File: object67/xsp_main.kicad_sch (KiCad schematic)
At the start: 66 parts, among them IC5 TPS7A4701RGWT, IC6 TPS7A3301RGWR, J2 PJ-037A, J3 Power In, J4 216700-0249, U10 ADP5070AREZ, U11 TPS62912, U7 TPS7A2050PDQNR, U8 TPS7A2033PDQNR, U9 TPS7A2033PDQNR

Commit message: Finished layout
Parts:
- added H1: MountingHole_Pad, MountingHole:MountingHole_4.3mm_M4_ISO7380_Pad_TopOnly, symbol Mechanical:MountingHole_Pad
- C59, C60, C62, C63, C64, C65, C67, C68, C69, C71, C75, C76, C77: footprint (none) -> Capacitor_SMD:C_0603_1608Metric
- C61, C66, C70: value 47u -> 10u; footprint (none) -> Capacitor_SMD:C_0603_1608Metric
- C72, C88, C89, C90, C92, C93: footprint (none) -> Capacitor_SMD:C_1206_3216Metric
- C73, C74, C80, C91: footprint (none) -> Capacitor_SMD:C_0402_1005Metric
- C78, C79, C81, C82, C83, C84, C85, C86, C87: footprint (none) -> Capacitor_SMD:C_0805_2012Metric
- D1, D2: footprint (none) -> Diode_SMD:D_PowerDI-123
- FB4: footprint (none) -> Inductor_SMD:L_0603_1608Metric
- J3: footprint (none) -> Connector_PinHeader_2.54mm:PinHeader_1x01_P2.54mm_Vertical
- J4: footprint 2167000249 -> object67:2167000249
- L1, L2, L3: footprint (none) -> Inductor_SMD:L_Wuerth_MAPI-4030
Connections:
- net +3.3V: now also J4.16, J4.17, J4.18, J4.19, J4.20
- net BICK_{ADC}: now also J4.7
- net BICK_{DAC}: now also J4.2
- net CLK_44.1_EN: now also J4.12
- net CLK_48_EN: now also J4.13
- net CLK_EN: now also J4.11
- net GNDD: now also J4.14, J4.15, J4.21, J4.22, J4.23, J4.24, J4.25 (MP_1), J4.26 (MP_2), J4.27 (MP_3), J4.28 (MP_4), J4.29 (MP_5), J4.30 (MP_6)
- net GNDPWR: now also H1.1
- net INT_{ADC}: now also J4.10
- net LRCK_{ADC}: now also J4.8
- net LRCK_{DAC}: now also J4.4
- net PDN_{DAC}: now also J4.1
- net SCL: now also J4.5
- net SDA: now also J4.6
- net SDATA_{ADC}: now also J4.9
- net SDATA_{DAC}: now also J4.3
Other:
- moved on the sheet: J4

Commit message: Start layout
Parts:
- added J5: 216700-0249, object67:2167000249, symbol object67:216700-0249
- added J6: Conn_02x08_Odd_Even, Connector_PinHeader_2.54mm:PinHeader_2x08_P2.54mm_Horizontal, symbol Connector_Generic:Conn_02x08_Odd_Even
- J3: footprint Connector_PinHeader_2.54mm:PinHeader_1x01_P2.54mm_Vertical -> TestPoint:TestPoint_2Pads_Pitch5.08mm_Drill1.3mm
- R35, R36, R37, R38, R39, R40, R42, R43, R44, R45: footprint (none) -> Resistor_SMD:R_0805_2012Metric
- R41: footprint (none) -> Resistor_SMD:R_0603_1608Metric
- TP1, TP2, TP3, TP4: footprint (none) -> TestPoint:TestPoint_Pad_D2.0mm
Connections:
- net +3.3V: now also J4.1, J4.2, J4.3, J4.4, J5.1, J5.16, J5.17, J5.2, J6.1 (Pin_1), J6.2 (Pin_2), J6.3 (Pin_3); no longer J4.19, J4.20
- net BICK_{ADC}: now also J5.3, J6.4 (Pin_4); no longer J4.7
- net BICK_{DAC}: now also J4.6, J6.7 (Pin_7); no longer J4.2
- net CLK_44.1_EN: now also J5.19, J6.14 (Pin_14); no longer J4.12
- net CLK_48_EN: now also J5.20, J6.16 (Pin_16); no longer J4.13
- net CLK_EN: now also J5.18, J6.12 (Pin_12); no longer J4.11
- net GNDD: now also J4.10, J4.11, J4.12, J4.13, J5.10, J5.11, J5.12, J5.13, J5.14, J5.15, J5.21, J5.22, J5.23, J5.24, J5.7, J5.8, J5.9, J6.15 (Pin_15); no longer J4.25 (MP_1), J4.26 (MP_2), J4.27 (MP_3), J4.28 (MP_4), J4.29 (MP_5), J4.30 (MP_6)
- net INT_{ADC}: now also J5.6, J6.10 (Pin_10); no longer J4.10
- net LRCK_{ADC}: now also J5.4, J6.6 (Pin_6); no longer J4.8
- net LRCK_{DAC}: now also J4.8, J6.11 (Pin_11); no longer J4.4
- net PDN_{DAC}: now also J4.5, J6.5 (Pin_5); no longer J4.1
- net SCL: now also J4.19; no longer J4.5
- net SDA: now also J4.20; no longer J4.6
- net SDATA_{ADC}: now also J5.5, J6.8 (Pin_8); no longer J4.9
- net SDATA_{DAC}: now also J4.7, J6.9 (Pin_9); no longer J4.3
- new net MLCK_{MCU}: J4.9, J6.13 (Pin_13)
- no-connect marks 22 -> 34

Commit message: Updated pcb
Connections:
- net GNDD is gone; now on net GND: C67.2, C68.2, C69.2, C70.2, C71.1, C73.1, C74.1, C75.2, J4.10, J4.11, J4.12, J4.13, J4.14, J4.15, J4.21, J4.22, J4.23, J4.24, J5.10, J5.11, J5.12, J5.13, J5.14, J5.15, J5.21, J5.22, J5.23, J5.24, J5.7, J5.8, J5.9, J6.15 (Pin_15), R38.1, U10.15 (AGND), U10.21 (AGND), U10.4 (SYNC/FREQ), U9.2 (GND), U9.5 (Pad)
- net GNDPWR is gone; now on net GND: C72.1, C76.1, C77.1, C78.1, C79.1, C80.1, C81.1, C82.1, C83.1, C84.1, C85.1, C86.1, H1.1, J2.1, J3.2 (Pin_2), L2.1, R41.1, R43.1, U10.1 (PGND), U11.4 (PGND), U11.7 (PSNS)
- net GNDA renamed GND

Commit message: Layout for ADP5070
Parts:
- C72: footprint Capacitor_SMD:C_1206_3216Metric -> Capacitor_SMD:C_0805_2012Metric
- C73, C74: footprint Capacitor_SMD:C_0402_1005Metric -> Capacitor_SMD:C_0603_1608Metric
- C76, C77: footprint Capacitor_SMD:C_0603_1608Metric -> Capacitor_SMD:C_1206_3216Metric
- R35, R36, R37: footprint Resistor_SMD:R_0805_2012Metric -> Resistor_SMD:R_0603_1608Metric
- U10: footprint Package_SO:ETSSOP-20-1EP_4.4x6.5mm_P0.65mm_EP3x4.2mm -> object67:SOP65P640X120-21N
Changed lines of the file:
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@@
 			)
 		)
-		(property "Footprint" "Resistor_SMD:R_0805_2012Metric"
+		(property "Footprint" "Resistor_SMD:R_0603_1608Metric"
 			(at 59.69 60.96 0)
 			(effects
@@
 			)
 		)
-		(property "Footprint" "Capacitor_SMD:C_0402_1005Metric"
+		(property "Footprint" "Capacitor_SMD:C_0603_1608Metric"
 			(at 52.07 40.64 0)
 			(effects
@@
 			)
 		)
-		(property "Footprint" "Resistor_SMD:R_0805_2012Metric"
+		(property "Footprint" "Resistor_SMD:R_0603_1608Metric"
 			(at 59.69 40.64 0)
 			(effects
@@
 			)
 		)
-		(property "Footprint" "Capacitor_SMD:C_1206_3216Metric"
+		(property "Footprint" "Capacitor_SMD:C_0805_2012Metric"
 			(at 39.37 59.69 0)
 			(effects
@@
 			)
 		)
-		(property "Footprint" "Resistor_SMD:R_0805_2012Metric"
+		(property "Footprint" "Resistor_SMD:R_0603_1608Metric"
 			(at 107.95 50.8 0)
 			(effects
@@
 			)
 		)
-		(property "Footprint" "Capacitor_SMD:C_0603_1608Metric"
+		(property "Footprint" "Capacitor_SMD:C_1206_3216Metric"
 			(at 121.92 57.15 0)
 			(effects
@@
 			)
 		)
-		(property "Footprint" "Package_SO:ETSSOP-20-1EP_4.4x6.5mm_P0.65mm_EP3x4.2mm"
+		(property "Footprint" "object67:SOP65P640X120-21N"
 			(at 80.01 86.36 0)
 			(effects
@@
 			)
 		)
-		(property "Footprint" "Capacitor_SMD:C_0603_1608Metric"
+		(property "Footprint" "Capacitor_SMD:C_1206_3216Metric"
 			(at 114.3 80.01 0)
 			(effects
@@
 			)
 		)
-		(property "Footprint" "Capacitor_SMD:C_0402_1005Metric"
+		(property "Footprint" "Capacitor_SMD:C_0603_1608Metric"
 			(at 52.07 60.96 0)
 			(effects

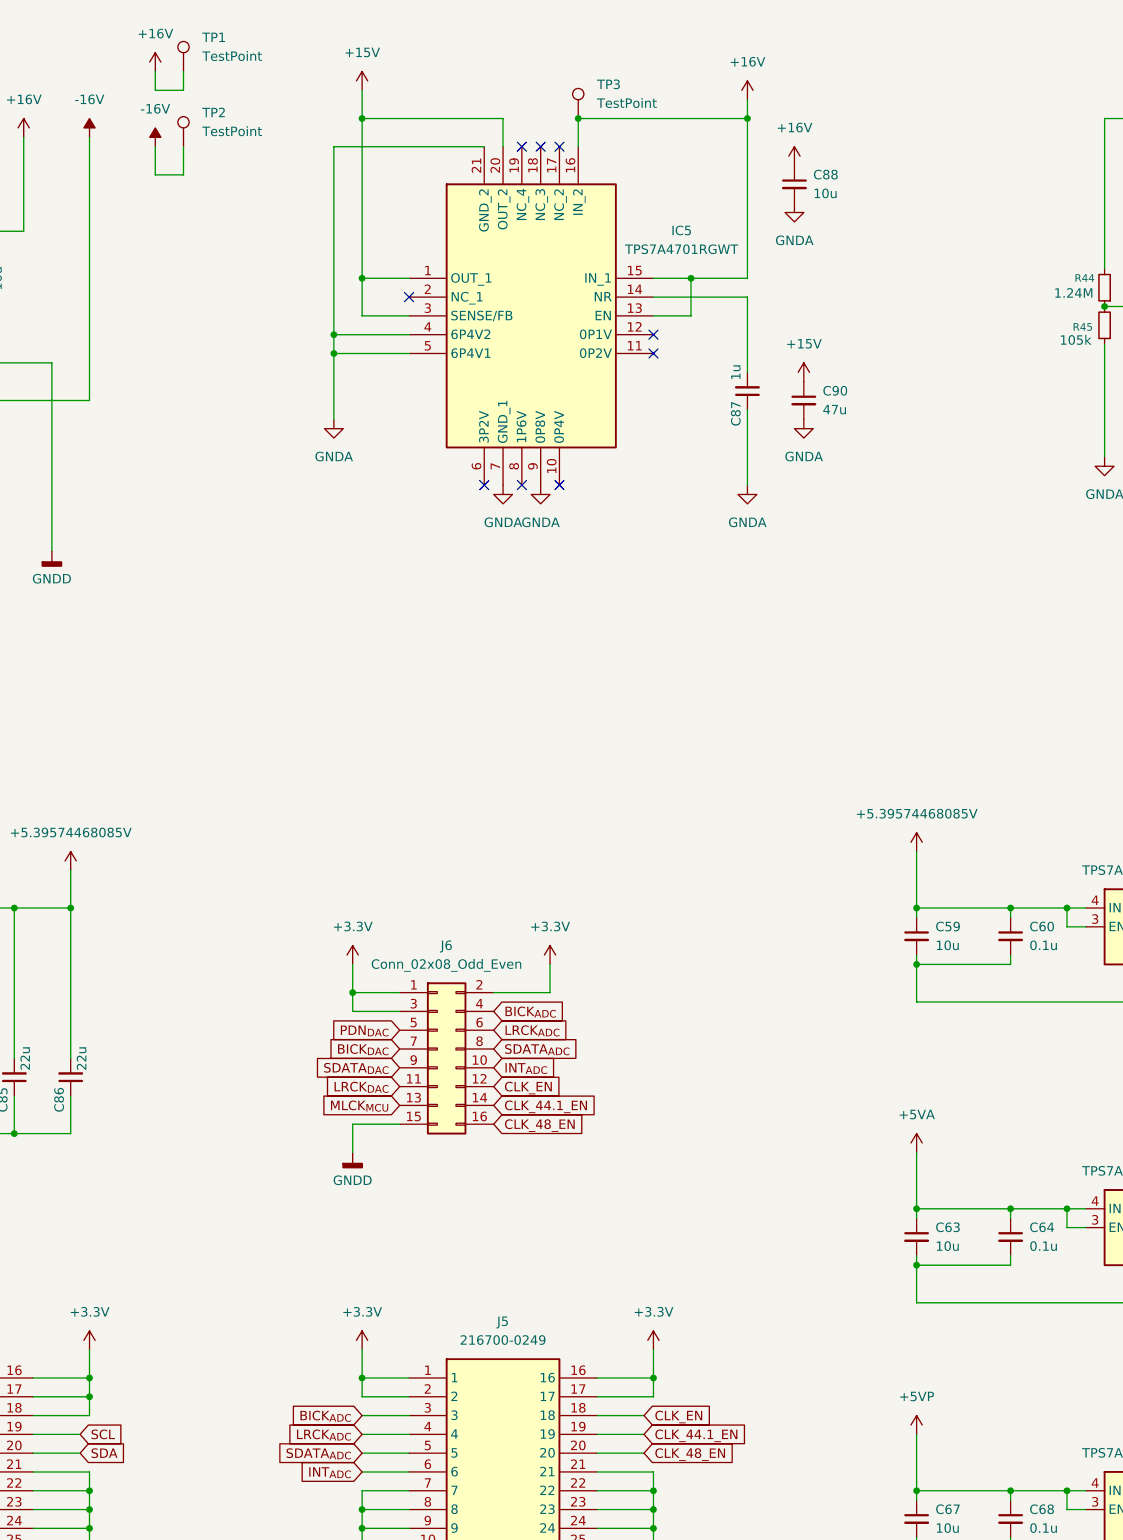
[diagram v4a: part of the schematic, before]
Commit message: Finished layout for ADC DAC, starting filter
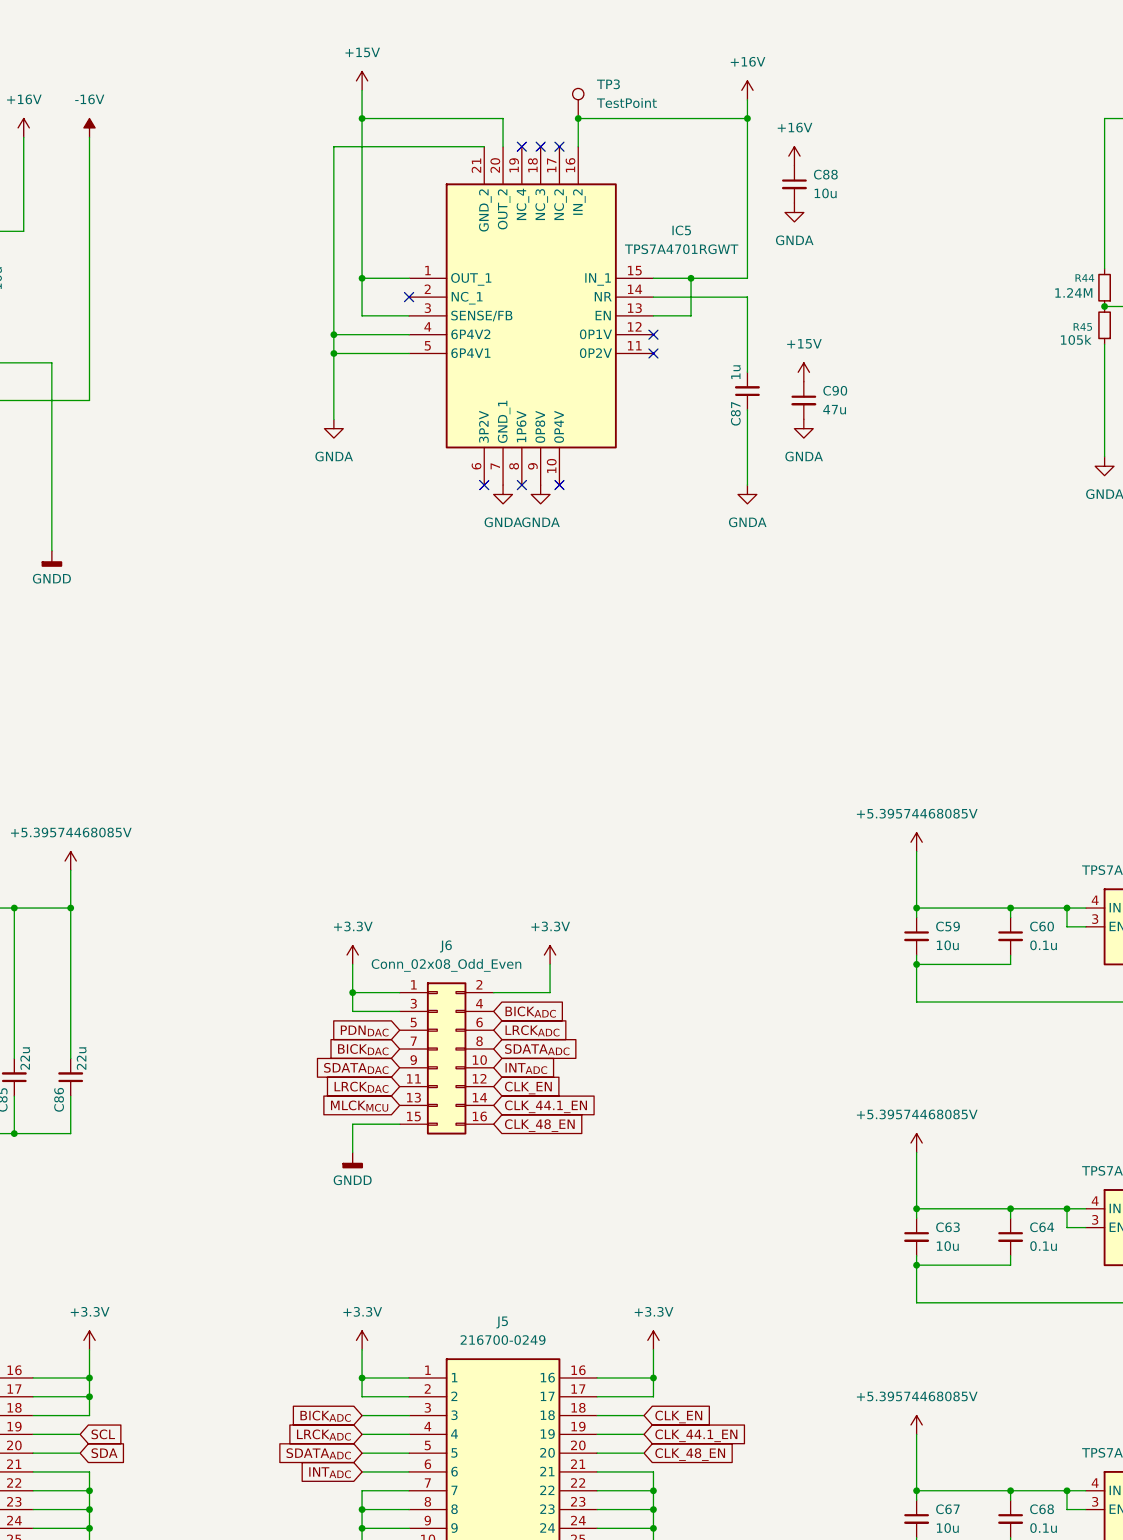
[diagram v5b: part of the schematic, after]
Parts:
- removed TP1, TP2: TestPoint, TestPoint:TestPoint_Pad_D2.0mm, symbol Connector:TestPoint
- R42, R43: footprint Resistor_SMD:R_0805_2012Metric -> Resistor_SMD:R_0603_1608Metric
- TP3, TP4: footprint TestPoint:TestPoint_Pad_D2.0mm -> TestPoint:TestPoint_Pad_D1.0mm
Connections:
- net +5VP is gone; now on net +5.39574468085V: C67.1, C68.1, U9.3 (EN), U9.4 (IN)
- net +5.39574468085V: now also C63.1, C64.1, U8.3 (EN), U8.4 (IN)
- net +5VA: no longer C63.1, C64.1, U8.3 (EN), U8.4 (IN)

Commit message: Filter
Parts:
- J6: footprint Connector_PinHeader_2.54mm:PinHeader_2x08_P2.54mm_Horizontal -> Connector_PinHeader_2.54mm:PinHeader_2x08_P2.54mm_Vertical
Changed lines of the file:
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@@
 			)
 		)
-		(property "Footprint" "Connector_PinHeader_2.54mm:PinHeader_2x08_P2.54mm_Horizontal"
+		(property "Footprint" "Connector_PinHeader_2.54mm:PinHeader_2x08_P2.54mm_Vertical"
 			(at 182.88 158.75 0)
 			(effects

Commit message: Filter
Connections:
- net GND: now also IC6.21 (GND_2), IC6.7 (GND_1)
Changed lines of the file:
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@@
 	)
 	(junction
+		(at 273.05 67.31)
+		(diameter 0)
+		(color 0 0 0 0)
+	)
+	(junction
 		(at 212.09 223.52)
 		(diameter 0)
@@
 	)
 	(junction
+		(at 273.05 73.66)
+		(diameter 0)
+		(color 0 0 0 0)
+	)
+	(junction
 		(at 97.79 71.12)
 		(diameter 0)
@@
 	(wire
 		(pts
+			(xy 273.05 73.66) (xy 273.05 92.71)
+		)
+		(stroke
+			(width 0)
+			(type default)
+		)
+	)
+	(wire
+		(pts
 			(xy 295.91 147.32) (xy 295.91 146.05)
 		)
@@
 	(wire
 		(pts
+			(xy 275.59 35.56) (xy 275.59 67.31)
+		)
+		(stroke
+			(width 0)
+			(type default)
+		)
+	)
+	(wire
+		(pts
 			(xy 52.07 161.29) (xy 52.07 170.18)
 		)
@@
 	(wire
 		(pts
+			(xy 299.72 81.28) (xy 299.72 86.36)
+		)
+		(stroke
+			(width 0)
+			(type default)
+		)
+	)
+	(wire
+		(pts
 			(xy 256.54 262.89) (xy 256.54 271.78)
 		)
@@
 	(wire
 		(pts
+			(xy 279.4 73.66) (xy 273.05 73.66)
+		)
+		(stroke
+			(width 0)
+			(type default)
+		)
+	)
+	(wire
+		(pts
 			(xy 36.83 170.18) (xy 43.18 170.18)
 		)
@@
 	(wire
 		(pts
+			(xy 279.4 86.36) (xy 279.4 73.66)
+		)
+		(stroke
+			(width 0)
+			(type default)
+		)
+	)
+	(wire
+		(pts
 			(xy 118.11 139.7) (xy 125.73 139.7)
 		)
@@
 	(wire
 		(pts
+			(xy 275.59 67.31) (xy 273.05 67.31)
+		)
+		(stroke
+			(width 0)
+			(type default)
+		)
+	)
+	(wire
+		(pts
 			(xy 96.52 228.6) (xy 96.52 226.06)
 		)
@@
 	(wire
 		(pts
+			(xy 294.64 35.56) (xy 275.59 35.56)
+		)
+		(stroke
+			(width 0)
+			(type default)
+		)
+	)
+	(wire
+		(pts
 			(xy 59.69 50.8) (xy 39.37 50.8)
 		)
@@
 	(wire
 		(pts
-			(xy 273.05 53.34) (xy 273.05 33.02)
+			(xy 308.61 152.4) (xy 308.61 147.32)
 		)
 		(stroke
@@
 	(wire
 		(pts
-			(xy 308.61 152.4) (xy 308.61 147.32)
+			(xy 247.65 147.32) (xy 247.65 152.4)
 		)
 		(stroke
@@
 	(wire
 		(pts
-			(xy 247.65 147.32) (xy 247.65 152.4)
+			(xy 100.33 154.94) (xy 93.98 154.94)
 		)
 		(stroke
@@
 	(wire
 		(pts
-			(xy 100.33 154.94) (xy 93.98 154.94)
+			(xy 317.5 58.42) (xy 321.31 58.42)
 		)
 		(stroke
@@
 	(wire
 		(pts
-			(xy 317.5 58.42) (xy 321.31 58.42)
+			(xy 172.72 236.22) (xy 179.07 236.22)
 		)
 		(stroke
@@
 	(wire
 		(pts
-			(xy 172.72 236.22) (xy 179.07 236.22)
+			(xy 95.25 203.2) (xy 95.25 205.74)
 		)
 		(stroke
@@
 	(wire
 		(pts
-			(xy 95.25 203.2) (xy 95.25 205.74)
+			(xy 93.98 68.58) (xy 102.87 68.58)
 		)
 		(stroke
@@
 	(wire
 		(pts
-			(xy 93.98 68.58) (xy 102.87 68.58)
+			(xy 273.05 67.31) (xy 273.05 73.66)
 		)
 		(stroke
@@
 	(wire
 		(pts
+			(xy 273.05 33.02) (xy 273.05 53.34)
+		)
+		(stroke
+			(width 0)
+			(type default)
+		)
+	)
+	(wire
+		(pts
 			(xy 171.45 151.13) (xy 171.45 153.67)
 		)
@@
 	(wire
 		(pts
-			(xy 273.05 63.5) (xy 273.05 78.74)
+			(xy 273.05 63.5) (xy 273.05 67.31)
 		)
 		(stroke
@@
 	(wire
 		(pts
+			(xy 299.72 86.36) (xy 279.4 86.36)
+		)
+		(stroke
+			(width 0)
+			(type default)
+		)
+	)
+	(wire
+		(pts
 			(xy 171.45 153.67) (xy 177.8 153.67)
 		)
@@
 	(symbol
 		(lib_id "power:GNDA")
-		(at 273.05 78.74 0)
+		(at 273.05 92.71 0)
 		(unit 1)
 		(exclude_from_sim no)
@@
 		(fields_autoplaced yes)
 		(property "Reference" "#PWR087"
-			(at 273.05 85.09 0)
+			(at 273.05 99.06 0)
 			(effects
 				(font
@@
 		)
 		(property "Value" "GNDA"
-			(at 273.05 83.82 0)
+			(at 273.05 97.79 0)
 			(effects
 				(font
@@
 		)
 		(property "Footprint" ""
-			(at 273.05 78.74 0)
+			(at 273.05 92.71 0)
 			(effects
 				(font
@@
 		)
 		(property "Datasheet" ""
-			(at 273.05 78.74 0)
+			(at 273.05 92.71 0)
 			(effects
 				(font
@@
 		)
 		(property "Description" "Power symbol creates a global label with name \"GNDA\" , analog ground"
-			(at 273.05 78.74 0)
+			(at 273.05 92.71 0)
 			(effects
 				(font

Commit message: Finished layout, start MCU
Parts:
- R38, R39, R40: footprint Resistor_SMD:R_0805_2012Metric -> Resistor_SMD:R_0603_1608Metric
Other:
- added sheet MCU (mcu.kicad_sch)
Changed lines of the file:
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@@
 			)
 		)
-		(property "Footprint" "Resistor_SMD:R_0805_2012Metric"
+		(property "Footprint" "Resistor_SMD:R_0603_1608Metric"
 			(at 99.06 64.77 0)
 			(effects
@@
 			)
 		)
-		(property "Footprint" "Resistor_SMD:R_0805_2012Metric"
+		(property "Footprint" "Resistor_SMD:R_0603_1608Metric"
 			(at 99.06 53.34 0)
 			(effects
@@
 			)
 		)
-		(property "Footprint" "Resistor_SMD:R_0805_2012Metric"
+		(property "Footprint" "Resistor_SMD:R_0603_1608Metric"
 			(at 106.68 68.58 0)
 			(effects
@@
 	)
 	(sheet
-		(at 344.17 209.55)
-		(size 55.88 34.29)
+		(at 360.68 218.44)
+		(size 39.37 25.4)
 		(exclude_from_sim no)
 		(in_bom yes)
@@
 		)
 		(property "Sheetname" "Motor Controller"
-			(at 344.17 208.8384 0)
+			(at 360.68 217.7284 0)
 			(effects
 				(font
@@
 		)
 		(property "Sheetfile" "motor.kicad_sch"
-			(at 344.17 244.4246 0)
+			(at 360.68 244.4246 0)
 			(effects
 				(font
@@
 	)
 	(sheet
-		(at 342.9 162.56)
-		(size 55.88 36.83)
+		(at 360.68 187.96)
+		(size 39.37 24.13)
 		(exclude_from_sim no)
 		(in_bom yes)
@@
 		)
 		(property "Sheetname" "Analog Frontend"
-			(at 342.9 161.8484 0)
+			(at 360.68 187.2484 0)
 			(effects
 				(font
@@
 		)
 		(property "Sheetfile" "frontend.kicad_sch"
-			(at 342.9 199.9746 0)
+			(at 360.68 212.6746 0)
 			(effects
 				(font
@@
 	)
 	(sheet
-		(at 344.17 120.65)
-		(size 55.88 31.75)
+		(at 360.68 154.94)
+		(size 39.37 27.94)
 		(exclude_from_sim no)
 		(in_bom yes)
@@
 		)
 		(property "Sheetname" "Audio"
-			(at 344.17 119.9384 0)
+			(at 360.68 154.2284 0)
 			(effects
 				(font
@@
 		)
 		(property "Sheetfile" "audio.kicad_sch"
-			(at 344.17 152.9846 0)
+			(at 360.68 183.4646 0)
 			(effects
 				(font
@@
 				)
 			)
+		)
+	)
+	(sheet
+		(at 360.68 121.92)
+		(size 39.37 24.13)
+		(exclude_from_sim no)
+		(in_bom yes)
+		(on_board yes)
+		(dnp no)
+		(fields_autoplaced yes)
+		(stroke
+			(width 0.1524)
+			(type solid)
+		)
+		(fill
+			(color 0 0 0 0.0000)
+		)
+		(property "Sheetname" "MCU"
+			(at 360.68 121.2084 0)
+			(effects
+				(font
+					(size 1.27 1.27)
+				)
+				(justify left bottom)
+			)
+		)
+		(property "Sheetfile" "mcu.kicad_sch"
+			(at 360.68 146.6346 0)
+			(effects
+				(font
+					(size 1.27 1.27)
+				)
+				(justify left top)
+			)
+		)
+		(instances
+			(project "object67"
+				(path "/a52a93a9-ab60-414c-847b-3047ce4056cf/2d7be8e2-05a1-49f5-8994-604be09973f2"
+					(page "6")
+				)
+			)
